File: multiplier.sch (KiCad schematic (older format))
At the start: 46 parts, among them Q10 BC557, Q11 BC557, Q12 BC557, Q13 BC557, Q19 BUT11, Q20 BC547B, Q3 BC557, Q4 BC557, Q5 BC547B, Q6 BC557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

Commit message: progress on schematics
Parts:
- removed Q20: BC547B, Package_TO_SOT_THT:TO-92_Inline, symbol 0_project:BC547B
- added C1: elko, symbol 0_project:elko
- added D1, D2, D5: 1N5400, Diode_THT:D_DO-201AD_P15.24mm_Horizontal, symbol 0_project:1N5401
- added D3: 1N5401, Diode_THT:D_DO-201AD_P15.24mm_Horizontal, symbol 0_project:1N5401
- added Q1: IRFZ34N, Package_DirectFET:DirectFET_MX, symbol 0_project:IRFZ34N
- added R1: 0, Resistor_THT:R_Axial_DIN0207_L6.3mm_D2.5mm_P2.54mm_Vertical, symbol Device:R
- S_IB_0, S_VE_2: Spice_Netlist_Enabled Y -> N
- S_IB_1, S_VE_0: Spice_Netlist_Enabled N -> Y
- V3: Spice_Model dc 0 ac 0 pwl(0 15 5 15) -> dc 0 ac 0 0 sin(0 15 60 0 0)
- Z4: renamed from D4; value D_Zener -> 5V
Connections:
- net 0: now also C1.2, D1.1 (K), D2.1 (K), Q1.3 (S), R1.2; no longer V3.2 (-)
- net SI0_+15V: now also C1.1, D3.2 (A), D5.2 (A); no longer V3.1 (+)
- net at R26.2: now also Q1.1 (D)
- net at R34.2: now also Q1.2 (G), R1.1
- new net: D1.2 (A), D3.1 (K), V3.1 (+)
- new net: D2.2 (A), D5.1 (K), V3.2 (-)
- no-connect marks 0 -> 5
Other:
- note added: ".options SAVECURRENTS TRTOL=1\n.tran 10u 5\n*.dc V3 0 20 2\n.print time"
- note removed: ".options SAVECURRENTS TRTOL=1\n.tran 200u 5\n*.dc V3 0 20 2\n.print time"
- moved on the sheet: V3
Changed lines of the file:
@@
 $Descr A4 11693 8268
 encoding utf-8
-Sheet 3 3
+Sheet 1 1
 Title ""
 Date ""
@@
 Text GLabel 7050 2875 0    50   UnSpc ~ 0
 SI0_B
-Text GLabel 8475 2675 0    50   UnSpc ~ 0
+Text GLabel 8475 2625 0    50   UnSpc ~ 0
 SI0_C
-Text GLabel 8475 3075 0    50   UnSpc ~ 0
+Text GLabel 8450 3075 0    50   UnSpc ~ 0
 SI0_E
-Text GLabel 10625 5325 1    50   UnSpc ~ 0
+Text GLabel 4400 6650 2    50   UnSpc ~ 0
 SI0_+15V
 $Comp
@@
 $EndComp
 Wire Wire Line
-	10625 5725 10625 5625
-Wire Wire Line
 	1075 3375 1075 3500
 $Comp
-L 0_project:D_Zener D4
+L 0_project:D_Zener Z4
 U 1 1 5E71C317
 P 1075 3750
-F 0 "D4" V 1029 3829 50  0000 L CNN
-F 1 "D_Zener" H 1075 3650 50  0001 C CNN
+F 0 "Z4" V 1075 3825 50  0000 L CNN
+F 1 "5V" V 1075 3650 50  0000 C CNN
 F 2 "Diode_THT:D_DO-35_SOD27_P2.54mm_Vertical_AnodeUp" H 1075 3750 50  0001 C CNN
 F 3 "~" H 1075 3750 50  0001 C CNN
@@
 	1    0    0    -1
 $EndComp
-$Comp
-L 0_project:BC547B Q20
-U 1 1 5E702FD7
-P 10500 3450
-F 0 "Q20" H 10691 3496 50  0000 L CNN
-F 1 "BC547B" H 10691 3405 50  0000 L CNN
-F 2 "Package_TO_SOT_THT:TO-92_Inline" H 10700 3375 50  0001 L CIN
-F 3 "http://www.fairchildsemi.com/ds/BC/BC547.pdf" H 10500 3450 50  0001 L CNN
-F 4 "Q" H 10700 3525 50  0001 L CNN "Spice_Primitive"
-F 5 "BC547B" H 10700 3525 50  0001 L CNN "Spice_Model"
-F 6 "Y" H 10700 3525 50  0001 L CNN "Spice_Netlist_Enabled"
-F 7 "/code/electronic/spice_lib/bjt.lib" H 10700 3525 50  0001 L CNN "Spice_Lib_File"
-	1    10500 3450
-	1    0    0    -1
-$EndComp
 Text GLabel 10600 2950 1    50   UnSpc ~ 0
 SI0_+15V
 Text Notes 8725 1375 0    50   ~ 0
-.options SAVECURRENTS TRTOL=1\n.tran 200u 5\n*.dc V3 0 20 2\n.print time
+.options SAVECURRENTS TRTOL=1\n.tran 10u 5\n*.dc V3 0 20 2\n.print time
 $Comp
 L Device:R R12
@@
 	10600 3650 10600 3950
 Wire Wire Line
-	9900 3950 10600 3950
+	9900 3950 10300 3950
 Wire Wire Line
 	9900 3450 9975 3450
@@
 U 1 1 5E6D3AA3
 P 9425 5050
-F 0 "IC_0" H 9150 4925 50  0000 R CNN
+F 0 "IC_0" H 9250 4950 50  0000 R CNN
 F 1 "VSOURCE" H 9059 5078 50  0001 R CNN
 F 2 "" H 9425 5050 50  0001 C CNN
@@
 F 3 "~" H 5850 6075 50  0001 C CNN
 F 4 "V" H 5850 6075 50  0001 C CNN "Spice_Primitive"
-F 5 "N" H 8375 5650 50  0000 C CNN "Spice_Netlist_Enabled"
+F 5 "Y" H 8375 5650 50  0000 C CNN "Spice_Netlist_Enabled"
 F 6 "dc 0 ac 0 pwl(0  20 0.1 20 3 20 3.1 2 5 2)" H 7350 5650 50  0000 C CNN "Spice_Model"
 	1    5850 6075
@@
 F 3 "~" H 6725 6025 50  0001 C CNN
 F 4 "V" H 6725 6025 50  0001 C CNN "Spice_Primitive"
-F 5 "Y" H 10125 5575 50  0000 C CNN "Spice_Netlist_Enabled"
+F 5 "N" H 10125 5575 50  0000 C CNN "Spice_Netlist_Enabled"
 F 6 "dc 0 ac 0 pwl(0 20 0.1 20  2 20  5 2)" H 9200 5575 50  0000 C CNN "Spice_Model"
 	1    6725 6025
@@
 F 3 "~" H 7200 4850 50  0001 C CNN
 F 4 "I" H 7200 4850 50  0001 C CNN "Spice_Primitive"
-F 5 "Y" H 3375 4625 50  0000 C CNN "Spice_Netlist_Enabled"
+F 5 "N" H 3375 4625 50  0000 C CNN "Spice_Netlist_Enabled"
 F 6 "dc 0 ac 0 pwl(0 10m 0.1 10m  2 500m  5 500m)" H 3625 4625 50  0000 L CNN "Spice_Model"
 	1    7200 4850
@@
 U 1 1 5E6E7719
 P 9425 5475
-F 0 "S_VC_0" H 9653 5521 50  0000 L CNN
+F 0 "S_VC_0" H 9050 5325 50  0000 L CNN
 F 1 "VSOURCE" H 9653 5430 50  0001 L CNN
 F 2 "" H 9425 5475 50  0001 C CNN
@@
 	-1   0    0    1
 $EndComp
-$Comp
-L 0_project:V V3
-U 1 1 5E75498C
-P 10625 5475
-F 0 "V3" H 10853 5521 50  0000 L CNN
-F 1 "VSOURCE" H 10853 5430 50  0001 L CNN
-F 2 "" H 10625 5475 50  0001 C CNN
-F 3 "~" H 10625 5475 50  0001 C CNN
-F 4 "V" H 10625 5475 50  0001 C CNN "Spice_Primitive"
-F 5 "Y" H 10625 5475 50  0001 C CNN "Spice_Netlist_Enabled"
-F 6 "dc 0 ac 0 pwl(0 15 5 15)" H 10725 4875 50  0000 C CNN "Spice_Model"
-	1    10625 5475
-	-1   0    0    1
-$EndComp
 Text GLabel 850  6150 0    50   UnSpc ~ 0
 SI_GND
@@
 Text Notes 6450 5250 0    50   ~ 0
 base control [A]
-Text Notes 10950 4800 2    50   ~ 0
+Text Notes 3825 6275 2    50   ~ 0
 fan control PSU\n
 Text Notes 9775 4575 2    50   ~ 0
@@
 Wire Wire Line
 	9425 5725 9875 5725
-Connection ~ 10050 5725
-Wire Wire Line
-	10050 5725 10625 5725
 Text GLabel 9875 5850 2    50   UnSpc ~ 0
 0
@@
 F 3 "~" H 6300 4925 50  0001 C CNN
 F 4 "I" H 6300 4925 50  0001 C CNN "Spice_Primitive"
-F 5 "N" H 3375 4700 50  0000 C CNN "Spice_Netlist_Enabled"
+F 5 "Y" H 3375 4700 50  0000 C CNN "Spice_Netlist_Enabled"
 F 6 "dc 0 ac 0 pwl(0 10m 0.1 10m  3 500m  3.1 0  5 500m)" H 3625 4675 50  0000 L CNN "Spice_Model"
 	1    6300 4925
@@
 Wire Notes Line
 	3050 5000 5900 5000
+$Comp
+L 0_project:1N5401 D3
+U 1 1 5E8E6C8B
+P 3800 6650
+F 0 "D3" H 3800 6475 50  0000 C CNN
+F 1 "1N5401" H 3800 6161 50  0001 C CNN
+F 2 "Diode_THT:D_DO-201AD_P15.24mm_Horizontal" H 3800 6475 50  0001 C CNN
+F 3 "http://www.vishay.com/docs/88516/1n5400.pdf" H 3800 6650 50  0001 C CNN
+F 4 "/var/src/electronic/spice_lib/diode.lib" H 3800 6252 50  0001 C CNN "Spice_Lib_File"
+F 5 "1N5401" H 3800 6550 50  0000 C CNN "Spice_Model"
+F 6 "Y" H 3800 6434 50  0001 C CNN "Spice_Netlist_Enabled"
+F 7 "D" H 3800 6525 50  0001 C CNN "Spice_Primitive"
+	1    3800 6650
+	-1   0    0    1
+$EndComp
+$Comp
+L 0_project:1N5401 D1
+U 1 1 5E8E92FD
+P 3350 6800
+F 0 "D1" V 3250 6650 50  0000 L CNN
+F 1 "1N5400" V 3213 6879 50  0001 L CNN
+F 2 "Diode_THT:D_DO-201AD_P15.24mm_Horizontal" H 3350 6625 50  0001 C CNN
+F 3 "http://www.vishay.com/docs/88516/1n5400.pdf" H 3350 6800 50  0001 C CNN
+F 4 "/var/src/electronic/spice_lib/diode.lib" V 3304 6879 50  0001 L CNN "Spice_Lib_File"
+F 5 "1N5401" V 3325 6450 50  0000 L CNN "Spice_Model"
+F 6 "Y" V 3486 6879 50  0001 L CNN "Spice_Netlist_Enabled"
+F 7 "D" V 3577 6879 50  0001 L CNN "Spice_Primitive"
+	1    3350 6800
+	0    1    1    0
+$EndComp
+$Comp
+L 0_project:1N5401 D2
+U 1 1 5E8EDED3
+P 3500 6950
+F 0 "D2" H 3500 7050 50  0000 C CNN
+F 1 "1N5400" H 3500 6461 50  0001 C CNN
+F 2 "Diode_THT:D_DO-201AD_P15.24mm_Horizontal" H 3500 6775 50  0001 C CNN
+F 3 "http://www.vishay.com/docs/88516/1n5400.pdf" H 3500 6950 50  0001 C CNN
+F 4 "/var/src/electronic/spice_lib/diode.lib" H 3500 6552 50  0001 C CNN "Spice_Lib_File"
+F 5 "1N5401" H 3450 7000 50  0000 C CNN "Spice_Model"
+F 6 "Y" H 3500 6734 50  0001 C CNN "Spice_Netlist_Enabled"
+F 7 "D" H 3500 6825 50  0001 C CNN "Spice_Primitive"
+	1    3500 6950
+	-1   0    0    1
+$EndComp
+$Comp
+L 0_project:1N5401 D5
+U 1 1 5E8EE8A6
+P 3950 6800
+F 0 "D5" V 3904 6879 50  0000 L CNN
+F 1 "1N5400" V 3995 6879 50  0001 L CNN
+F 2 "Diode_THT:D_DO-201AD_P15.24mm_Horizontal" H 3950 6625 50  0001 C CNN
+F 3 "http://www.vishay.com/docs/88516/1n5400.pdf" H 3950 6800 50  0001 C CNN
+F 4 "D" H 3950 6800 50  0001 C CNN "Spice_Primitive"
+F 5 "D1N5401" V 4000 7025 50  0000 C CNN "Spice_Model"
+F 6 "Y" H 3950 6800 50  0001 C CNN "Spice_Netlist_Enabled"
+F 7 "/var/src/electronic/spice_lib/diode.lib" H 3950 6800 50  0001 C CNN "Spice_Lib_File"
+	1    3950 6800
+	0    1    1    0
+$EndComp
+$Comp
+L 0_project:V V3
+U 1 1 5E75498C
+P 3650 6800
+F 0 "V3" H 3725 6700 50  0000 L CNN
+F 1 "VSOURCE" H 3878 6755 50  0001 L CNN
+F 2 "" H 3650 6800 50  0001 C CNN
+F 3 "~" H 3650 6800 50  0001 C CNN
+F 4 "V" H 3650 6800 50  0001 C CNN "Spice_Primitive"
+F 5 "Y" H 3650 6800 50  0001 C CNN "Spice_Netlist_Enabled"
+F 6 "dc 0 ac 0 0 sin(0 15 60 0 0)" H 3500 6325 50  0000 C CNN "Spice_Model"
+	1    3650 6800
+	-1   0    0    1
+$EndComp
+Wire Wire Line
+	3950 6950 3650 6950
+Connection ~ 3650 6950
+Wire Wire Line
+	3650 6650 3350 6650
+Connection ~ 3650 6650
+Text GLabel 3350 6950 0    50   UnSpc ~ 0
+0
+$Comp
+L 0_project:IRFZ34N Q1
+U 1 1 5E95BF21
+P 10500 3450
+F 0 "Q1" H 10704 3496 50  0000 L CNN
+F 1 "IRFZ34N" H 10700 3450 50  0001 L CNN
+F 2 "Package_DirectFET:DirectFET_MX" H 10500 3450 50  0001 C CIN
+F 3 "https://www.infineon.com/dgdl/Infineon-BSB008NE2LX-DS-v02_00-EN.pdf?fileId=db3a30432e564707012e5745ca7d000e" H 10500 3450 50  0001 L CNN
+F 4 "M" H 10700 3525 50  0001 L CNN "Spice_Primitive"
+F 5 "IRFZ34N" H 10704 3405 50  0000 L CNN "Spice_Model"
+F 6 "Y" H 10700 3525 50  0001 L CNN "Spice_Netlist_Enabled"
+F 7 "/var/src/electronic/spice/spice_lib/mosfet.lib" H 10700 3525 50  0001 L CNN "Spice_Lib_File"
+	1    10500 3450
+	1    0    0    -1
+$EndComp
+$Comp
+L Device:R R1
+U 1 1 5E95EB50
+P 10300 3700
+F 0 "R1" H 10370 3746 50  0000 L CNN
+F 1 "0" H 10370 3655 50  0001 L CNN
+F 2 "Resistor_THT:R_Axial_DIN0207_L6.3mm_D2.5mm_P2.54mm_Vertical" V 10230 3700 50  0001 C CNN
+F 3 "~" H 10300 3700 50  0001 C CNN
+F 4 "Y" H 10300 3700 50  0001 C CNN "Spice_Netlist_Enabled"
+F 5 "50k" H 10400 3675 50  0000 C CNN "Spice_Model"
+F 6 "R" H 10300 3700 50  0001 C CNN "Spice_Primitive"
+	1    10300 3700
+	1    0    0    -1
+$EndComp
+Wire Wire Line
+	10300 3550 10300 3450
+Wire Wire Line
+	10300 3850 10300 3950
+Connection ~ 10300 3950
+Wire Wire Line
+	10300 3950 10600 3950
+Connection ~ 10300 3450
+$Comp
+L 0_project:elko C1
+U 1 1 5E97ABBD
+P 4150 7275
+F 0 "C1" V 3950 7275 50  0000 C CNN
+F 1 "elko" V 4250 7125 50  0001 C CNN
+F 2 "" H 4150 7275 50  0001 C CNN
+F 3 "~" H 4150 7275 50  0001 C CNN
+F 4 "X" V 4250 7425 50  0001 C CNN "Spice_Primitive"
+F 5 "elko_1u_leaky" V 4350 7275 50  0000 C CNN "Spice_Model"
+F 6 "Y" V 4250 7425 50  0001 C CNN "Spice_Netlist_Enabled"
+F 7 "/var/src/electronic/spice_lib/elko.lib" V 4250 7425 50  0001 C CNN "Spice_Lib_File"
+	1    4150 7275
+	0    1    1    0
+$EndComp
+Wire Wire Line
+	3900 7275 3350 7275
+Wire Wire Line
+	3350 7275 3350 6950
+Connection ~ 3350 6950
+Wire Wire Line
+	4400 7275 4400 6650
+Wire Wire Line
+	4400 6650 3950 6650
+Connection ~ 3950 6650
+NoConn ~ 6875 4450
+NoConn ~ 6875 4400
+NoConn ~ 5000 4975
+NoConn ~ 5350 4700
+NoConn ~ 4450 4675
+Wire Wire Line
+	8450 3075 8475 3075
+Wire Wire Line
+	8475 2625 8475 2675
 $EndSCHEMATC

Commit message: footprint assoziation; pcb layout; and more
* delete mainboard pcb
* rearrange project files/names
* create pcb layout
* improve schematics
* more
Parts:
- removed R1: 0, Resistor_THT:R_Axial_DIN0207_L6.3mm_D2.5mm_P2.54mm_Vertical, symbol Device:R
- added R2: 50k, symbol Device:R
- added R?: 150, symbol Device:R
- added Z1: zener, Diode_THT:D_DO-35_SOD27_P2.54mm_Vertical_AnodeUp, symbol 0_project:D_Zener
- C1: footprint (none) -> Capacitor_THT:CP_Radial_D5.0mm_P2.50mm; Spice_Model elko_1u_leaky -> elko_10u_leaky
- D1, D2: value 1N5400 -> 1N4007; footprint Diode_THT:D_DO-201AD_P15.24mm_Horizontal -> (none); symbol 0_project:1N5401 -> Diode:1N4007; Spice_Model 1N5401 -> D1N4007
- D3: value 1N5401 -> 1N4007; footprint Diode_THT:D_DO-201AD_P15.24mm_Horizontal -> (none); symbol 0_project:1N5401 -> Diode:1N4007; Spice_Model 1N5401 -> D1N4007
- D5: value 1N5400 -> 1N4007; footprint Diode_THT:D_DO-201AD_P15.24mm_Horizontal -> Diode_THT:D_DO-41_SOD81_P2.54mm_Vertical_AnodeUp; symbol 0_project:1N5401 -> Diode:1N4007; Spice_Model D1N5401 -> D1N4007
- Q1: footprint Package_DirectFET:DirectFET_MX -> (none); Spice_Model IRFZ34N -> irfz34n_IR; Spice_Primitive M -> X
- Q10, Q11, Q13, Q3, Q4, Q6, Q7, Q8, Q9: footprint Package_TO_SOT_THT:TO-92L_Inline_Wide -> Package_TO_SOT_THT:TO-92_Inline_Wide
- Q19: footprint Package_TO_SOT_THT:TO-220-3_Vertical -> (none)
- Q5: footprint Package_TO_SOT_THT:TO-92_Inline -> Package_TO_SOT_THT:TO-92_Inline_Wide
- R26: value 200k -> 150; footprint Resistor_THT:R_Axial_DIN0207_L6.3mm_D2.5mm_P2.54mm_Vertical -> (none)
- R33, R34, R35, R36: footprint Resistor_THT:R_Axial_DIN0207_L6.3mm_D2.5mm_P2.54mm_Vertical -> (none)
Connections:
- net 0: now also R?.2; no longer C6.2, Q1.3 (S)
- net at Q1.2 (G), R34.2: now also R2.1
- new net: C6.2, Q1.3 (S), R?.1, Z1.1 (K)
- new net: R2.2, Z1.2 (A)
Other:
- note added: ".options SAVECURRENTS TRTOL=1\n.tran 200u 5\n*.dc V3 0 20 2\n.print time"
- note removed: ".options SAVECURRENTS TRTOL=1\n.tran 10u 5\n*.dc V3 0 20 2\n.print time"
- moved on the sheet: R42

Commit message: progress on schematics
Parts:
- C1: footprint Capacitor_THT:CP_Radial_D5.0mm_P2.50mm -> (none)
- D5: footprint Diode_THT:D_DO-41_SOD81_P2.54mm_Vertical_AnodeUp -> (none)
- Z1: footprint Diode_THT:D_DO-35_SOD27_P2.54mm_Vertical_AnodeUp -> (none)
- gave numbers to parts that had none: 1
- renumbered R2 to R1
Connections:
- net 0: no longer Q11.1 (C), Q8.1 (C), R13.1, R23.1, R25.1, R31.2, R39.2, R40.2, R41.2, R42.2, R7.2, Z4.1 (K)
- net SI0_+15V: no longer Q3.3 (E), Q6.3 (E), R8.1
- net SI0_B: no longer R24.1
- net SI0_C: no longer R12.1
- net SI0_E: no longer R22.1, R29.1
- net SI0_F+: no longer Q10.1 (C), Q13.1 (C)
- new net SI_+15V: Q3.3 (E), Q6.3 (E), R8.1
- new net SI_B: R24.1
- new net SI_C: R12.1
- new net SI_E: R22.1, R29.1
- new net SI_F+: Q10.1 (C), Q13.1 (C)
- new net SI_GND: Q11.1 (C), Q8.1 (C), R13.1, R23.1, R25.1, R31.2, R39.2, R40.2, R41.2, R42.2, R7.2, Z4.1 (K)
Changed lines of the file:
@@
 $Descr A4 11693 8268
 encoding utf-8
-Sheet 1 1
+Sheet 2 2
 Title ""
 Date ""
@@
 SI_GND
 Wire Wire Line
-	8175 1900 8175 1500
-Wire Wire Line
-	8075 1900 8075 1500
-Wire Wire Line
-	7775 1900 7775 1500
-Wire Wire Line
-	7675 1900 7675 1500
-Wire Wire Line
-	7975 1900 7975 1500
-Wire Wire Line
-	7875 1900 7875 1500
+	7350 1925 7350 1525
+Wire Wire Line
+	7250 1925 7250 1525
+Wire Wire Line
+	6950 1925 6950 1525
+Wire Wire Line
+	6850 1925 6850 1525
+Wire Wire Line
+	7150 1925 7150 1525
+Wire Wire Line
+	7050 1925 7050 1525
 Text GLabel 7875 1900 3    50   UnSpc ~ 0
 SI_GND
@@
 F 0 "D5" V 3904 6879 50  0000 L CNN
 F 1 "1N4007" V 3995 6879 50  0001 L CNN
-F 2 "Diode_THT:D_DO-41_SOD81_P2.54mm_Vertical_AnodeUp" H 3950 6625 50  0001 C CNN
+F 2 "" H 3950 6625 50  0001 C CNN
 F 3 "http://www.vishay.com/docs/88516/1n5400.pdf" H 3950 6800 50  0001 C CNN
 F 4 "D" H 3950 6800 50  0001 C CNN "Spice_Primitive"
@@
 F 0 "C1" V 3950 7275 50  0000 C CNN
 F 1 "elko" V 4250 7125 50  0001 C CNN
-F 2 "Capacitor_THT:CP_Radial_D5.0mm_P2.50mm" H 4150 7275 50  0001 C CNN
+F 2 "" H 4150 7275 50  0001 C CNN
 F 3 "~" H 4150 7275 50  0001 C CNN
 F 4 "X" V 4250 7425 50  0001 C CNN "Spice_Primitive"
@@
 F 0 "Z1" V 10300 4150 50  0000 L CNN
 F 1 "zener" V 10300 3975 50  0001 C CNN
-F 2 "Diode_THT:D_DO-35_SOD27_P2.54mm_Vertical_AnodeUp" H 10300 4075 50  0001 C CNN
+F 2 "" H 10300 4075 50  0001 C CNN
 F 3 "~" H 10300 4075 50  0001 C CNN
 F 4 "/var/src/electronic/spice/spice-lib/zener.lib" H 10300 4175 50  0001 C CNN "Spice_Lib_File"
@@
 $EndComp
 $Comp
-L Device:R R2
+L Device:R R1
 U 1 1 5EB15A6A
 P 10300 3775
-F 0 "R2" H 10370 3821 50  0000 L CNN
+F 0 "R1" H 10370 3821 50  0000 L CNN
 F 1 "50k" H 10370 3730 50  0001 L CNN
 F 2 "" V 10230 3775 50  0001 C CNN
@@
 $EndComp
 $Comp
-L Device:R R?
+L Device:R R5
 U 1 1 5EB22872
 P 10600 4675
-F 0 "R?" H 10670 4721 50  0000 L CNN
+F 0 "R5" H 10670 4721 50  0000 L CNN
 F 1 "150" H 10670 4630 50  0001 L CNN
 F 2 "" V 10530 4675 50  0001 C CNN

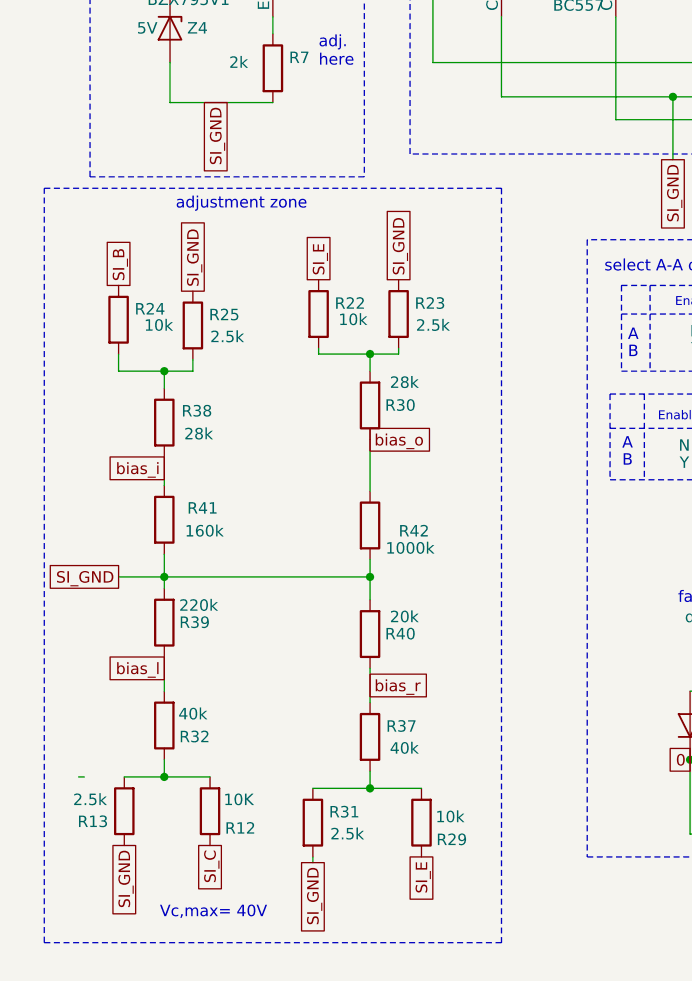
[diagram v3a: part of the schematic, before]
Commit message: add adjustment resistors
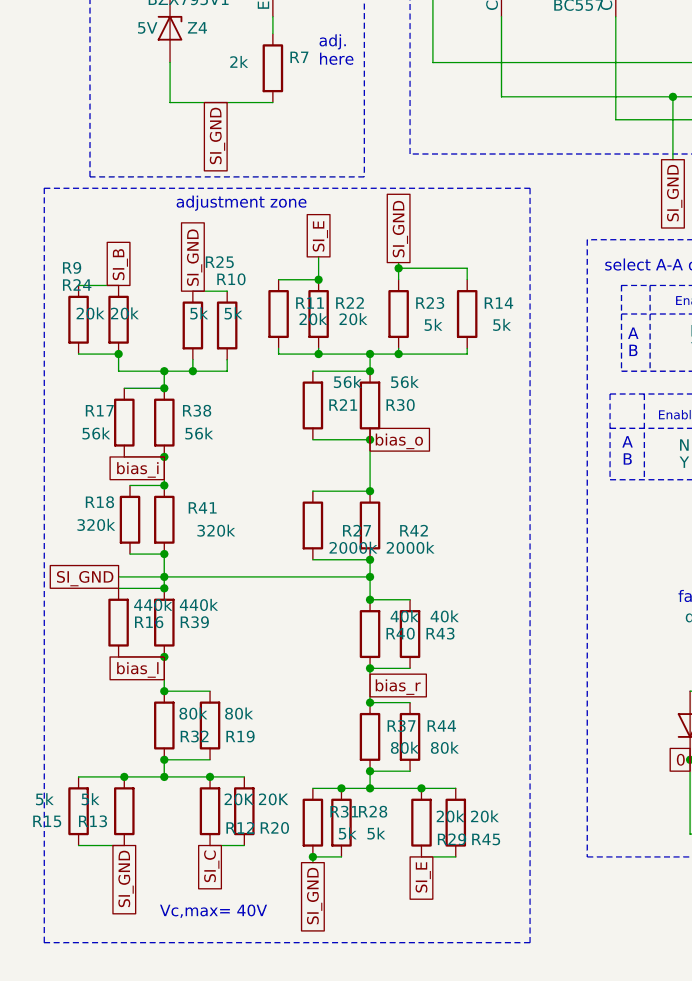
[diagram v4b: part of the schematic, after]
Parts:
- added R10, R16, R17, R18, R19, R21, R27, R43, R44: 100K, Resistor_THT:R_Axial_DIN0207_L6.3mm_D2.5mm_P2.54mm_Vertical, symbol Device:R
- added R11, R45: 150K, Resistor_THT:R_Axial_DIN0207_L6.3mm_D2.5mm_P2.54mm_Vertical, symbol Device:R
- added R14, R28: 50K, Resistor_THT:R_Axial_DIN0207_L6.3mm_D2.5mm_P2.54mm_Vertical, symbol Device:R
- added R15: 50k, Resistor_THT:R_Axial_DIN0207_L6.3mm_D2.5mm_P2.54mm_Vertical, symbol Device:R
- added R20: 150k, Resistor_THT:R_Axial_DIN0207_L6.3mm_D2.5mm_P2.54mm_Vertical, symbol Device:R
- added R9: 300K, Resistor_THT:R_Axial_DIN0207_L6.3mm_D2.5mm_P2.54mm_Vertical, symbol Device:R
- R12: Spice_Model 10K -> 20K
- R13, R23, R25, R31: Spice_Model 2.5k -> 5k
- R22, R24, R29: Spice_Model 10k -> 20k
- R30, R38: Spice_Model 28k -> 56k
- R32, R37: Spice_Model 40k -> 80k
- R39: Spice_Model 220k -> 440k
- R40: Spice_Model 20k -> 40k
- R41: Spice_Model 160k -> 320k
- R42: Spice_Model 1000k -> 2000k
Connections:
- net SI_B: now also R9.1
- net SI_C: now also R20.1
- net SI_E: now also R11.1, R45.1
- net SI_GND: now also R10.1, R14.1, R15.1, R16.2, R18.2, R27.2, R28.2, R43.2
- net bias_i: now also R17.2, R18.1
- net bias_l: now also R16.1, R19.2
- net bias_o: now also R21.1, R27.1
- net bias_r: now also R43.1, R44.1
- net at R24.2, R25.2, R38.1: now also R10.2, R17.1, R9.2
- net at R22.2, R23.2, R30.2: now also R11.2, R14.2, R21.2
- net at R12.2, R13.2, R32.1: now also R15.2, R19.1, R20.2
- net at R29.2, R31.1, R37.2: now also R28.1, R44.2, R45.2
